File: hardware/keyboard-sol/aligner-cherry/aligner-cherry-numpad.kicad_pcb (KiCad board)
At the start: 2 copper layers, 62.1 x 116.9 mm, 19 parts, among them SW67 NP Dash, SW68 NP 4, SW69 NP Zero, SW71 NP 7, SW72 NP 1, SW73 NP period, SW75 NP asterisk, SW76 NP 5, SW77 NP plus, SW79 NP 8, SW80 NP 2, SW82 NP divide, SW83 NP 6, SW85 NP 9, SW86 NP 3

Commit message: Moved mounting slots from keyboard PCB to aligners
- This allows the PCB to sink below the mounting brackets.  The aligner height can
be adjusted relative to the mounting brackets using spacers.

- changed futaba aligners to use cherry stabilizers.

- bumped rev number
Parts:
- removed the REF** at (187.9, 219.3)
- removed the REF** at (149.8, 219.3)
- removed the REF** at (187.9, 113.9)
- removed the REF** at (149.8, 113.9)
- added REF**: MountingHole_3.2mm_M3, MountingHole:MountingHole_3.2mm_M3, F.Cu at (432.4, 219.5)
- added REF**: MountingHole_3.2mm_M3, MountingHole:MountingHole_3.2mm_M3, F.Cu at (470.5, 219.5)
- added REF**: MountingHole_3.2mm_M3, MountingHole:MountingHole_3.2mm_M3, F.Cu at (470.5, 114.1)
- added REF**: MountingHole_3.2mm_M3, MountingHole:MountingHole_3.2mm_M3, F.Cu at (432.4, 114.1)
- moved SW67 282.6 mm to (432.4, 130.6)
- moved SW68 282.6 mm to (432.4, 168.7)
- moved SW69 282.6 mm to (432.4, 206.8)
- moved SW71 282.6 mm to (432.4, 149.6)
- moved SW72 282.6 mm to (432.4, 187.7)
- moved SW77 282.6 mm to (470.5, 206.8)
- moved SW82 282.6 mm to (470.5, 130.6)
- moved SW83 282.6 mm to (470.5, 168.7)
- moved SW85 282.6 mm to (470.5, 149.6)
- moved SW86 282.6 mm to (470.5, 187.7)
- moved SW73 282.6 mm to (451.5, 206.8)
- moved SW75 282.6 mm to (451.5, 130.6)
- moved SW76 282.6 mm to (451.5, 168.7)
- moved SW79 282.6 mm to (451.5, 149.6)
- moved SW80 282.6 mm to (451.5, 187.7)
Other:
- board size 62.1 x 116.9 mm -> 83.7 x 117.7 mm
- board text added: "SOL-20 Cherry MX aligner (numpad) Rev 1.1"
- board text added: "https://github.com/osiweb/unified_retro_keyboard Unified Keyboard Project"
- board text removed: "SOL-20 Cherry MX aligner (NumPad) Rev 1.0"
- board text removed: "https://github.com/osiweb/unified_retro_keyboard"
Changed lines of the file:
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@@
   (general
     (thickness 1.6)
-    (drawings 7)
+    (drawings 15)
     (tracks 0)
     (zones 0)
@@
     (title "Unified Retro Keyboard")
     (date 2019-08-25)
-    (rev 1.3)
+    (rev 1.1)
     (company OSIWeb.org)
-    (comment 1 "Key matrix w/ LED")
+    (comment 1 "Key aligner - Cherry (numpad)")
   )
   (layers
@@
       (drillshape 0)
       (scaleselection 1)
-      (outputdirectory "numpad-outputs"))
+      (outputdirectory "outputs"))
   )
   (net 0 "")
@@
   )
   (module unikbd:Key_MX_Aligner locked (layer F.Cu)
-    (at 168.85158 168.51376)
+    (at 451.47738 168.69156)
     (fp_text reference SW76 (at -5.7912 -8.6106) (layer F.SilkS)
       (effects (font (size 1 1) (thickness 0.15)))
@@
   )
   (module unikbd:Key_MX_Aligner locked (layer F.Cu)
-    (at 149.80158 168.51376)
+    (at 432.42738 168.69156)
     (fp_text reference SW68 (at -5.7912 -8.6106) (layer F.SilkS)
       (effects (font (size 1 1) (thickness 0.15)))
@@
   )
   (module unikbd:Key_MX_Aligner locked (layer F.Cu)
-    (at 187.90158 168.51376)
+    (at 470.52738 168.69156)
     (fp_text reference SW83 (at -5.7912 -8.6106) (layer F.SilkS)
       (effects (font (size 1 1) (thickness 0.15)))
@@
   )
   (module unikbd:Key_MX_Aligner locked (layer F.Cu)
-    (at 187.90158 149.46376)
+    (at 470.52738 149.64156)
     (fp_text reference SW85 (at -4.03098 -8.56996) (layer F.SilkS)
       (effects (font (size 1 1) (thickness 0.15)))
@@
   )
   (module unikbd:Key_MX_Aligner locked (layer F.Cu)
-    (at 187.90158 187.56376)
+    (at 470.52738 187.74156)
     (fp_text reference SW86 (at -5.7912 -8.6106) (layer F.SilkS)
       (effects (font (size 1 1) (thickness 0.15)))
@@
   )
   (module unikbd:Key_MX_Aligner locked (layer F.Cu)
-    (at 187.90158 130.41376)
+    (at 470.52738 130.59156)
     (fp_text reference SW82 (at -5.7912 -8.6106) (layer F.SilkS)
       (effects (font (size 1 1) (thickness 0.15)))
@@
   )
   (module unikbd:Key_MX_Aligner locked (layer F.Cu)
-    (at 168.85158 187.56376)
+    (at 451.47738 187.74156)
     (fp_text reference SW80 (at -5.7912 -8.6106) (layer F.SilkS)
       (effects (font (size 1 1) (thickness 0.15)))
@@
   )
   (module unikbd:Key_MX_Aligner locked (layer F.Cu)
-    (at 168.85158 149.46376)
+    (at 451.47738 149.64156)
     (fp_text reference SW79 (at -3.75158 -8.56996) (layer F.SilkS)
       (effects (font (size 1 1) (thickness 0.15)))
@@
   )
   (module unikbd:Key_MX_Aligner locked (layer F.Cu)
-    (at 187.90158 206.61376)
+    (at 470.52738 206.79156)
     (fp_text reference SW77 (at -5.7912 -8.6106) (layer F.SilkS)
       (effects (font (size 1 1) (thickness 0.15)))
@@
   )
   (module unikbd:Key_MX_Aligner locked (layer F.Cu)
-    (at 168.85158 130.41376)
+    (at 451.47738 130.59156)
     (fp_text reference SW75 (at -5.7912 -8.6106) (layer F.SilkS)
       (effects (font (size 1 1) (thickness 0.15)))
@@
   )
   (module unikbd:Key_MX_Aligner locked (layer F.Cu)
-    (at 168.85158 206.61376)
+    (at 451.47738 206.79156)
     (fp_text reference SW73 (at -5.7912 -8.6106) (layer F.SilkS)
       (effects (font (size 1 1) (thickness 0.15)))
@@
   )
   (module unikbd:Key_MX_Aligner locked (layer F.Cu)
-    (at 149.80158 187.56376)
+    (at 432.42738 187.74156)
     (fp_text reference SW72 (at -5.7912 -8.6106) (layer F.SilkS)
       (effects (font (size 1 1) (thickness 0.15)))
@@
   )
   (module unikbd:Key_MX_Aligner locked (layer F.Cu)
-    (at 149.80158 149.46376)
+    (at 432.42738 149.64156)
     (fp_text reference SW71 (at -5.7912 -8.6106) (layer F.SilkS)
       (effects (font (size 1 1) (thickness 0.15)))
@@
   )
   (module unikbd:Key_MX_Aligner locked (layer F.Cu)
-    (at 149.80158 206.61376)
+    (at 432.42738 206.79156)
     (fp_text reference SW69 (at -5.7912 -8.6106) (layer F.SilkS)
       (effects (font (size 1 1) (thickness 0.15)))
@@
   )
   (module unikbd:Key_MX_Aligner locked (layer F.Cu)
-    (at 149.80158 130.41376)
+    (at 432.42738 130.59156)
     (fp_text reference SW67 (at -5.7912 -8.6106) (layer F.SilkS)
       (effects (font (size 1 1) (thickness 0.15)))
@@
   )
   (module MountingHole:MountingHole_3.2mm_M3 locked (layer F.Cu)
-    (at 187.90158 219.31376)
+    (at 432.42738 219.49156)
     (descr "Mounting Hole 3.2mm, no annular, M3")
     (tags "mounting hole 3.2mm no annular m3")
     (attr virtual)
-    (fp_text reference REF** (at 0 -4.2) (layer F.SilkS)
+    (fp_text reference REF** (at 0 -4.2) (layer F.SilkS) hide
       (effects (font (size 1 1) (thickness 0.15)))
     )
@@
       (effects (font (size 1 1) (thickness 0.15)))
     )
+    (fp_text user %R (at 0.3 0) (layer F.Fab)
+      (effects (font (size 1 1) (thickness 0.15)))
+    )
+    (fp_circle (center 0 0) (end 3.2 0) (layer Cmts.User) (width 0.15))
     (fp_circle (center 0 0) (end 3.45 0) (layer F.CrtYd) (width 0.05))
-    (fp_circle (center 0 0) (end 3.2 0) (layer Cmts.User) (width 0.15))
-    (fp_text user %R (at 0.3 0) (layer F.Fab)
-      (effects (font (size 1 1) (thickness 0.15)))
-    )
     (pad 1 np_thru_hole circle (at 0 0) (size 3.2 3.2) (drill 3.2) (layers *.Cu *.Mask))
   )
   (module MountingHole:MountingHole_3.2mm_M3 locked (layer F.Cu)
-    (at 149.80158 219.31376)
+    (at 470.52738 219.49156)
     (descr "Mounting Hole 3.2mm, no annular, M3")
     (tags "mounting hole 3.2mm no annular m3")
     (attr virtual)
-    (fp_text reference REF** (at 0 -4.2) (layer F.SilkS)
+    (fp_text reference REF** (at 0 -4.2) (layer F.SilkS) hide
       (effects (font (size 1 1) (thickness 0.15)))
     )
@@
       (effects (font (size 1 1) (thickness 0.15)))
     )
+    (fp_text user %R (at 0.3 0) (layer F.Fab)
+      (effects (font (size 1 1) (thickness 0.15)))
+    )
+    (fp_circle (center 0 0) (end 3.2 0) (layer Cmts.User) (width 0.15))
     (fp_circle (center 0 0) (end 3.45 0) (layer F.CrtYd) (width 0.05))
-    (fp_circle (center 0 0) (end 3.2 0) (layer Cmts.User) (width 0.15))
-    (fp_text user %R (at 0.3 0) (layer F.Fab)
-      (effects (font (size 1 1) (thickness 0.15)))
-    )
     (pad 1 np_thru_hole circle (at 0 0) (size 3.2 3.2) (drill 3.2) (layers *.Cu *.Mask))
   )
   (module MountingHole:MountingHole_3.2mm_M3 locked (layer F.Cu)
-    (at 187.90158 113.90376)
+    (at 470.52738 114.08156)
     (descr "Mounting Hole 3.2mm, no annular, M3")
     (tags "mounting hole 3.2mm no annular m3")
     (attr virtual)
-    (fp_text reference REF** (at 0 -4.2) (layer F.SilkS)
+    (fp_text reference REF** (at 0 -4.2) (layer F.SilkS) hide
       (effects (font (size 1 1) (thickness 0.15)))
     )
@@
   )
   (module MountingHole:MountingHole_3.2mm_M3 locked (layer F.Cu)
-    (at 149.80158 113.90376)
+    (at 432.42738 114.08156)
     (descr "Mounting Hole 3.2mm, no annular, M3")
     (tags "mounting hole 3.2mm no annular m3")
     (attr virtual)
-    (fp_text reference REF** (at 0 -4.2) (layer F.SilkS)
+    (fp_text reference REF** (at 0 -4.2) (layer F.SilkS) hide
       (effects (font (size 1 1) (thickness 0.15)))
     )
@@
     (pad 1 np_thru_hole circle (at 0 0) (size 3.2 3.2) (drill 3.2) (layers *.Cu *.Mask))
   )
-  (gr_text https://github.com/osiweb/unified_retro_keyboard (at 198.1454 203.6826 90) (layer F.SilkS)
+  (gr_line (start 505.44984 200.12914) (end 505.44984 134.08914) (layer Edge.Cuts) (width 0.1016))
+  (gr_line (start 421.767 224.79) (end 421.767 107.0864) (layer Edge.Cuts) (width 0.1016))
+  (gr_text "SOL-20 Cherry MX aligner  (numpad)\nRev 1.1\n" (at 498.4496 195.834 90) (layer F.SilkS)
     (effects (font (size 2.032 2.032) (thickness 0.2032)) (justify left))
   )
-  (gr_text "SOL-20 Cherry MX aligner (NumPad) Rev 1.0" (at 139.5984 126.9746 270) (layer F.SilkS)
-    (effects (font (size 2.032 2.032) (thickness 0.2032)) (justify left))
-  )
-  (gr_line (start 137.8966 223.8502) (end 199.9742 223.8502) (layer Edge.Cuts) (width 0.1016))
-  (gr_line (start 137.8966 106.9086) (end 199.9742 106.9086) (layer Edge.Cuts) (width 0.1016))
-  (gr_line (start 199.9742 106.9086) (end 199.9742 223.8502) (layer Edge.Cuts) (width 0.1016))
-  (gr_line (start 137.8966 106.9086) (end 137.8966 223.8502) (layer Edge.Cuts) (width 0.1016))
+  (gr_text "https://github.com/osiweb/unified_retro_keyboard\nUnified Keyboard Project" (at 485.013 164.211 90) (layer F.SilkS)
+    (effects (font (size 2.032 2.032) (thickness 0.2032)))
+  )
   (gr_text "Key spacing guide:\nVertical: 0.75 inch.\n\nKey1, Key2  ->  Centers (inches)\n\n1.00,  1.00  ->  0.75\n1.00,  1.25  ->  0.84375\n1.00,  1.50  ->  0.9375\n1.00,  1.75  ->  1.03125\n1.00,  2.00  ->  1.125\n1.25,  1.25  ->  0.9375\n1.25,  1.50  ->  1.03125\n1.25,  2.00  ->  1.21875\n1.50,  1.50  ->  1.125\n1.50,  2.00  ->  1.3125\n1.75,  2.00. ->. 1.40625\n8.00,  1.00  ->  3.375\n8.00,  1.25  ->  3.46875\n8.00,  1.50  ->  3.5625" (at 78.1304 274.8788) (layer F.Mask)
     (effects (font (size 2.032 2.032) (thickness 0.3048)) (justify left))
   )
+  (gr_line (start 505.45238 107.0864) (end 505.45238 130.27914) (layer Edge.Cuts) (width 0.1016))
+  (gr_line (start 505.45238 224.79) (end 505.45238 203.93914) (layer Edge.Cuts) (width 0.1016))
+  (gr_line (start 488.78109 203.93914) (end 505.44984 203.93914) (layer Edge.Cuts) (width 0.1016))
+  (gr_line (start 488.78109 134.08914) (end 505.44984 134.08914) (layer Edge.Cuts) (width 0.1016))
+  (gr_line (start 488.78109 130.27914) (end 505.44984 130.27914) (layer Edge.Cuts) (width 0.1016))
+  (gr_arc (start 488.78109 132.18414) (end 488.78109 130.27914) (angle -180) (layer Edge.Cuts) (width 0.1016))
+  (gr_line (start 488.78109 200.12914) (end 505.44984 200.12914) (layer Edge.Cuts) (width 0.1016))
+  (gr_arc (start 488.78109 202.03414) (end 488.78109 200.12914) (angle -180) (layer Edge.Cuts) (width 0.1016))
+  (gr_line (start 421.767 224.79) (end 505.45238 224.79) (layer Edge.Cuts) (width 0.1))
+  (gr_line (start 505.45238 107.0864) (end 421.767 107.0864) (layer Edge.Cuts) (width 0.1016))
 )

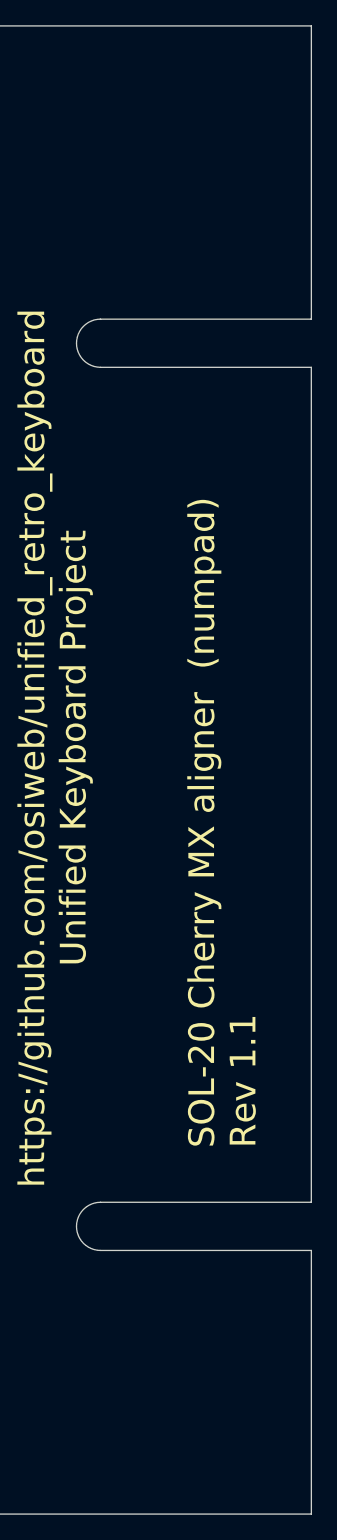
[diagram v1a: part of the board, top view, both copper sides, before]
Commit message: Adjsut mounting slots and alignment of mounting holes.
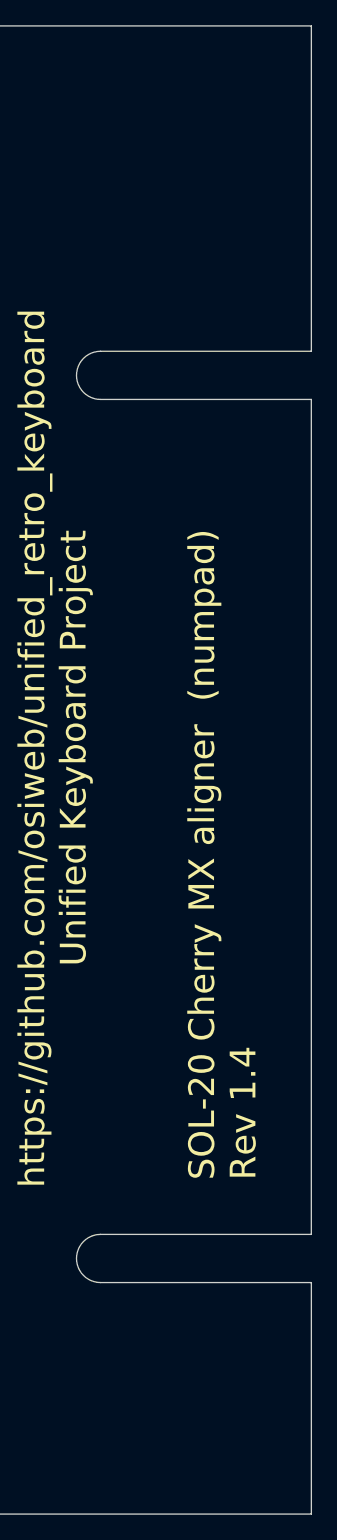
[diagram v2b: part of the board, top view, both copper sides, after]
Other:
- outline, holes or cut-outs redrawn
- board text added: "SOL-20 Cherry MX aligner (numpad) Rev 1.4"
- board text removed: "SOL-20 Cherry MX aligner (numpad) Rev 1.1"
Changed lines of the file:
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@@
     (pad 1 np_thru_hole circle (at 0 0) (size 3.2 3.2) (drill 3.2) (layers *.Cu *.Mask))
   )
-  (gr_line (start 505.44984 200.12914) (end 505.44984 134.08914) (layer Edge.Cuts) (width 0.1016))
+  (gr_line (start 505.44984 202.66914) (end 505.44984 136.62914) (layer Edge.Cuts) (width 0.1016))
   (gr_line (start 421.767 224.79) (end 421.767 107.0864) (layer Edge.Cuts) (width 0.1016))
-  (gr_text "SOL-20 Cherry MX aligner  (numpad)\nRev 1.1\n" (at 498.4496 195.834 90) (layer F.SilkS)
+  (gr_text "SOL-20 Cherry MX aligner  (numpad)\nRev 1.4\n" (at 498.4496 198.374 90) (layer F.SilkS)
     (effects (font (size 2.032 2.032) (thickness 0.2032)) (justify left))
   )
@@
     (effects (font (size 2.032 2.032) (thickness 0.3048)) (justify left))
   )
-  (gr_line (start 505.45238 107.0864) (end 505.45238 130.27914) (layer Edge.Cuts) (width 0.1016))
-  (gr_line (start 505.45238 224.79) (end 505.45238 203.93914) (layer Edge.Cuts) (width 0.1016))
-  (gr_line (start 488.78109 203.93914) (end 505.44984 203.93914) (layer Edge.Cuts) (width 0.1016))
-  (gr_line (start 488.78109 134.08914) (end 505.44984 134.08914) (layer Edge.Cuts) (width 0.1016))
-  (gr_line (start 488.78109 130.27914) (end 505.44984 130.27914) (layer Edge.Cuts) (width 0.1016))
-  (gr_arc (start 488.78109 132.18414) (end 488.78109 130.27914) (angle -180) (layer Edge.Cuts) (width 0.1016))
-  (gr_line (start 488.78109 200.12914) (end 505.44984 200.12914) (layer Edge.Cuts) (width 0.1016))
-  (gr_arc (start 488.78109 202.03414) (end 488.78109 200.12914) (angle -180) (layer Edge.Cuts) (width 0.1016))
+  (gr_line (start 505.45238 107.0864) (end 505.45238 132.81914) (layer Edge.Cuts) (width 0.1016))
+  (gr_line (start 505.45238 224.79) (end 505.45238 206.47914) (layer Edge.Cuts) (width 0.1016))
+  (gr_line (start 488.78109 206.47914) (end 505.44984 206.47914) (layer Edge.Cuts) (width 0.1016))
+  (gr_line (start 488.78109 136.62914) (end 505.44984 136.62914) (layer Edge.Cuts) (width 0.1016))
+  (gr_line (start 488.78109 132.81914) (end 505.44984 132.81914) (layer Edge.Cuts) (width 0.1016))
+  (gr_arc (start 488.78109 134.72414) (end 488.78109 132.81914) (angle -180) (layer Edge.Cuts) (width 0.1016))
+  (gr_line (start 488.78109 202.66914) (end 505.44984 202.66914) (layer Edge.Cuts) (width 0.1016))
+  (gr_arc (start 488.78109 204.57414) (end 488.78109 202.66914) (angle -180) (layer Edge.Cuts) (width 0.1016))
   (gr_line (start 421.767 224.79) (end 505.45238 224.79) (layer Edge.Cuts) (width 0.1))
   (gr_line (start 505.45238 107.0864) (end 421.767 107.0864) (layer Edge.Cuts) (width 0.1016))
